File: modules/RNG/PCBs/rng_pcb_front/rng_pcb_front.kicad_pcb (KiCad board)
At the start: 2 copper layers, 50 x 100 mm, 34 parts, among them J1 THONKICONN, J10 Conn_01x08_Pin, J2 THONKICONN, J3 THONKICONN, J4 THONKICONN, J5 THONKICONN, J6 THONKICONN, J7 Conn_01x07_Pin, J8 Conn_02x03_Socket, J9 Conn_01x06_Pin, SW1 RotaryEncoder_Switch, SW2 TAIWAY 200CWMSP1T3B4M2, SW3 TAIWAY 200CWMSP1T3B4M2

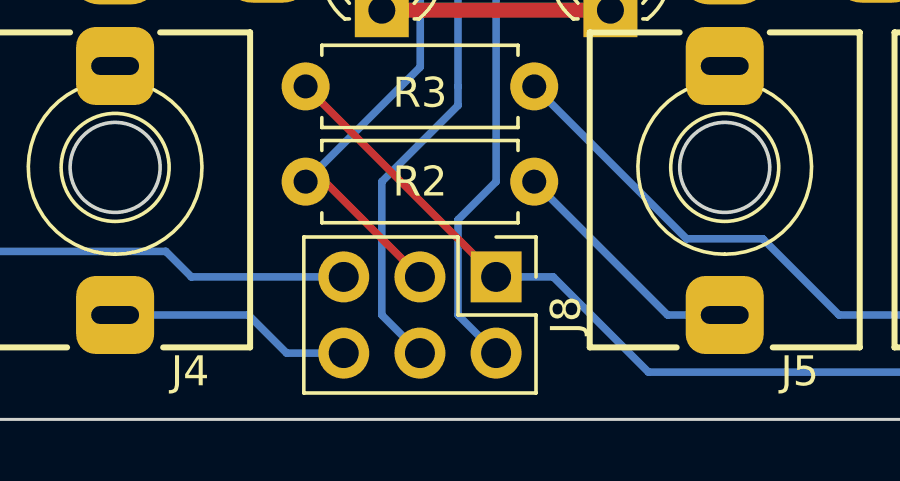
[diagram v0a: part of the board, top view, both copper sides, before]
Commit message: flip silkscreen for pin header
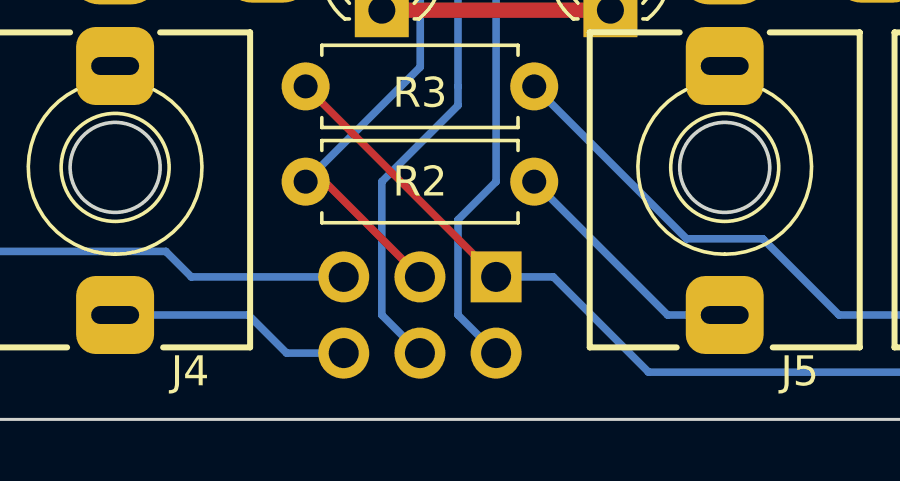
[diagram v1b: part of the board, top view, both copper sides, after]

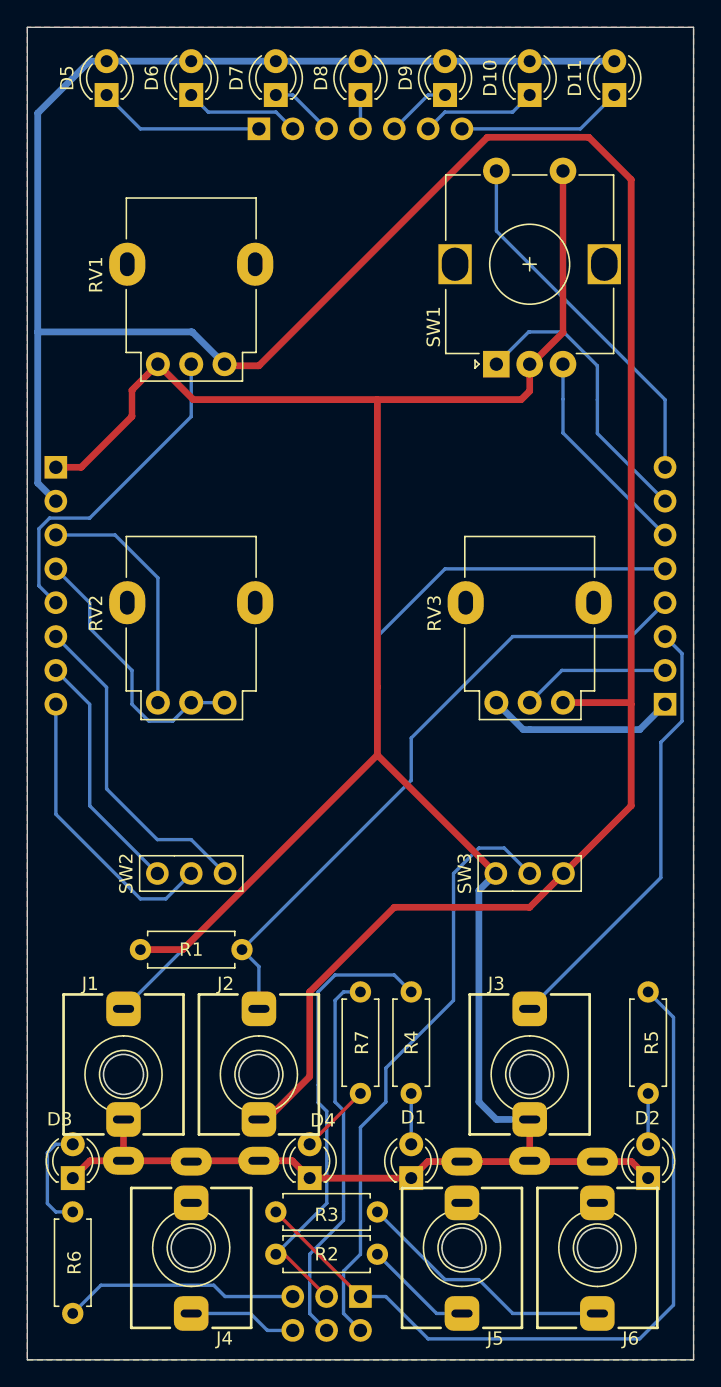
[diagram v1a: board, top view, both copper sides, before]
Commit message: add pulldown resistor to RNG clock input
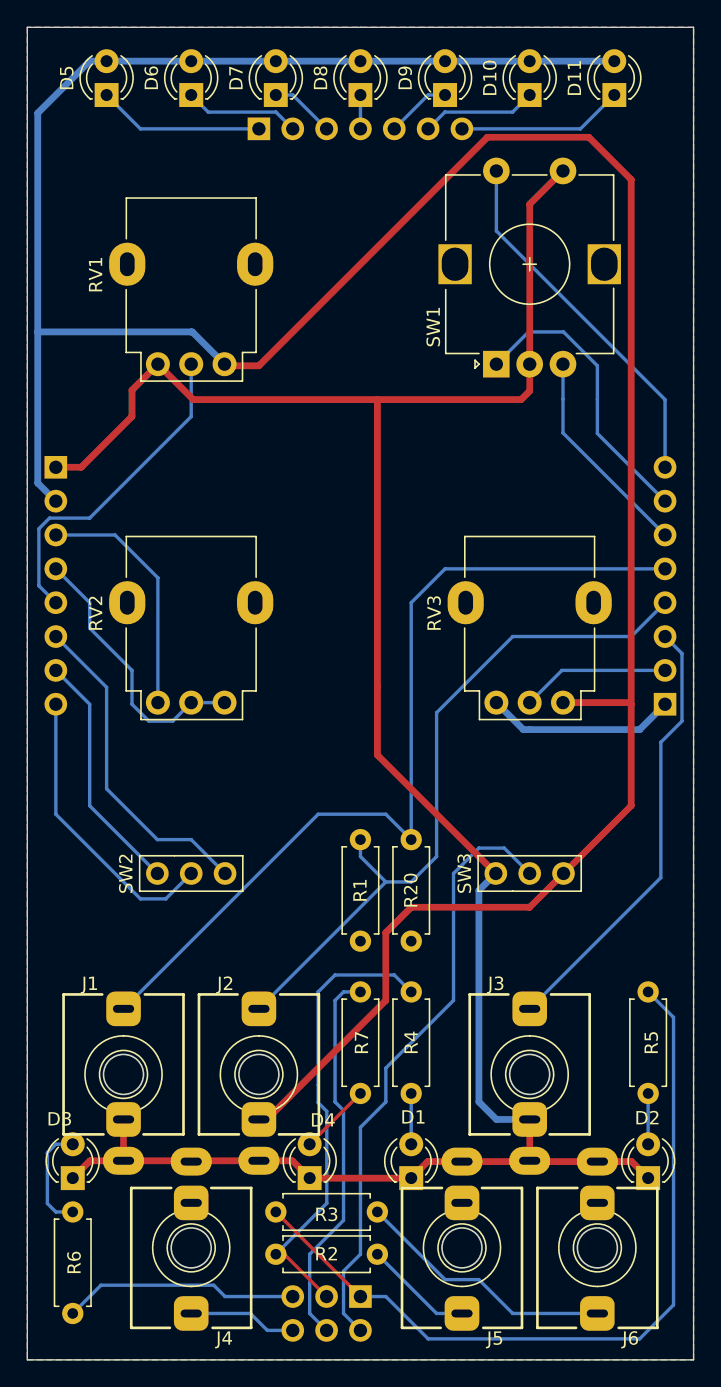
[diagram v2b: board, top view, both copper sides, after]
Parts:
- added R20: 100k, Resistor_THT:R_Axial_DIN0207_L6.3mm_D2.5mm_P7.62mm_Horizontal, F.Cu at (54.6, 111.8)
- moved R1 12.1 mm to (50.8, 111.8), turned to -90 degrees
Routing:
- net GND: track 209.7 -> 185.9 mm
- net INPUT_CV_CLOCK: track 59.5 -> 66.3 mm
- net INPUT_CV_ENABLE: track 49.4 -> 53.4 mm
- net +5V: track 221.9 -> 221.2 mm
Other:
- board text added: "FreeModular RNG front v3.1"
- board text removed: "FreeModular RNG front v3.0"

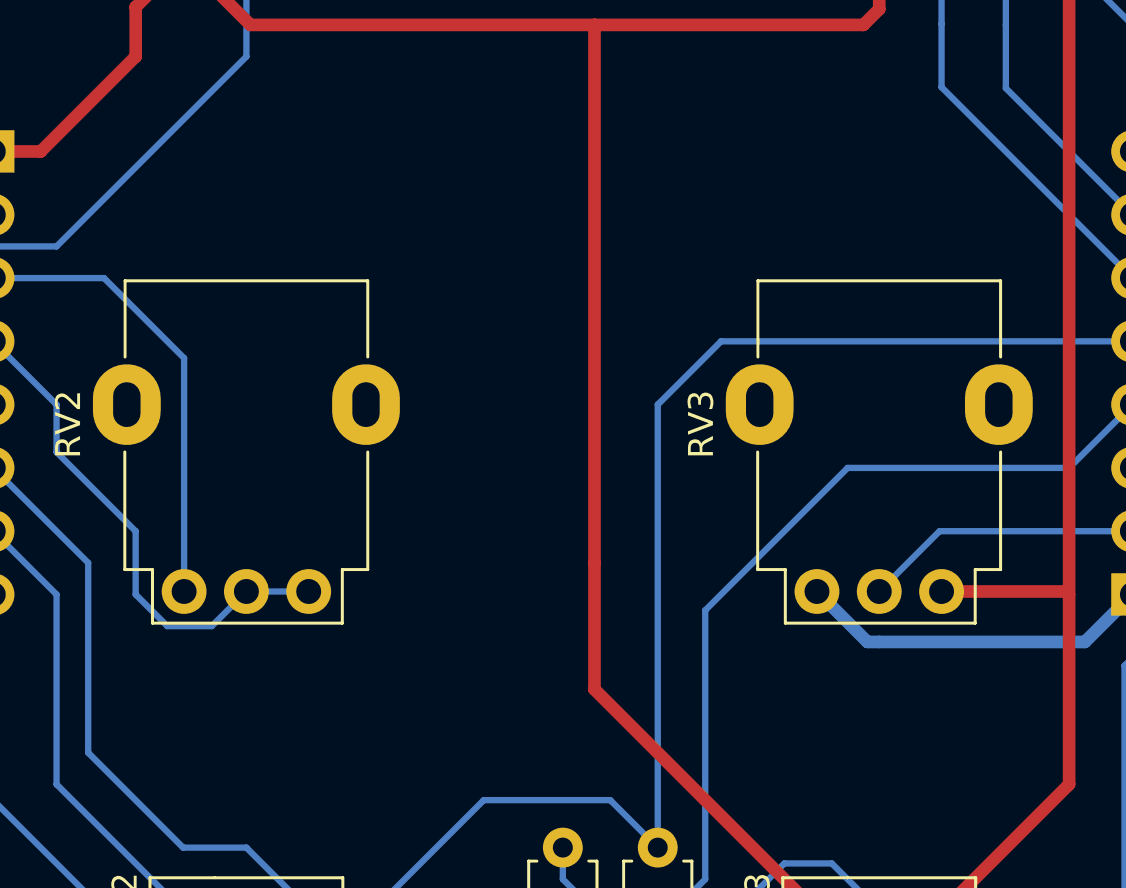
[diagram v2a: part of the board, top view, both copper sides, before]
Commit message: Add SMD option for LED driver on RNG
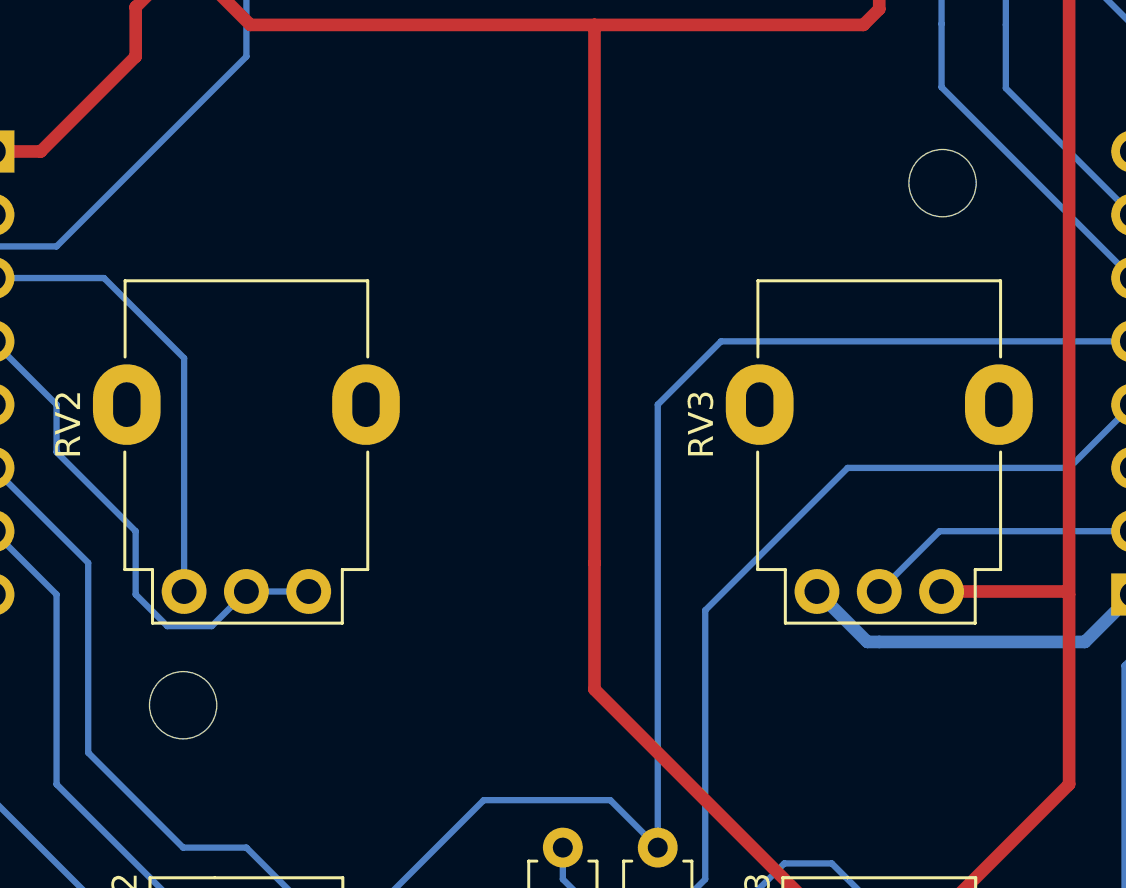
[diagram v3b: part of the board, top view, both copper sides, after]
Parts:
- added H1: M2.5, MountingHole:MountingHole_2.7mm_M2.5, F.Cu at (66.0, 85.1)
- added H2: M2.5, MountingHole:MountingHole_2.7mm_M2.5, F.Cu at (35.6, 106.0)
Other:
- board text added: "FreeModular RNG front v3.3"
- board text removed: "FreeModular RNG front v3.1"

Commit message: Update kicad files to reflect 8-pin connections instead of 6-pin.
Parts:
- J9: value Conn_01x06_Pin -> Conn_01x08_Pin
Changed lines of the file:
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@@
 			)
 		)
-		(property "Value" "Conn_01x06_Pin"
+		(property "Value" "Conn_01x08_Pin"
 			(at 0 -20.11 0)
 			(layer "B.Fab")
